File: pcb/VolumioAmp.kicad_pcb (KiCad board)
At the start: 2 copper layers, 136 x 71.2 mm, 81 parts, among them IC1 PCM2706, IC2 WM8804GEDS_V, J3 24v Input, Q1 DMP3013SFV-7, U1 74LVC1G07SE-7, U2 TPD4EUSB30, U3 TPD4EUSB30, U4 MagJack-A70-112-331N126, U5 FSUSB42MUX, U6 24AA02-OT, U7 AP64501SP-13, U8 LT1761-3.3, U9 MA12040PXUMA1

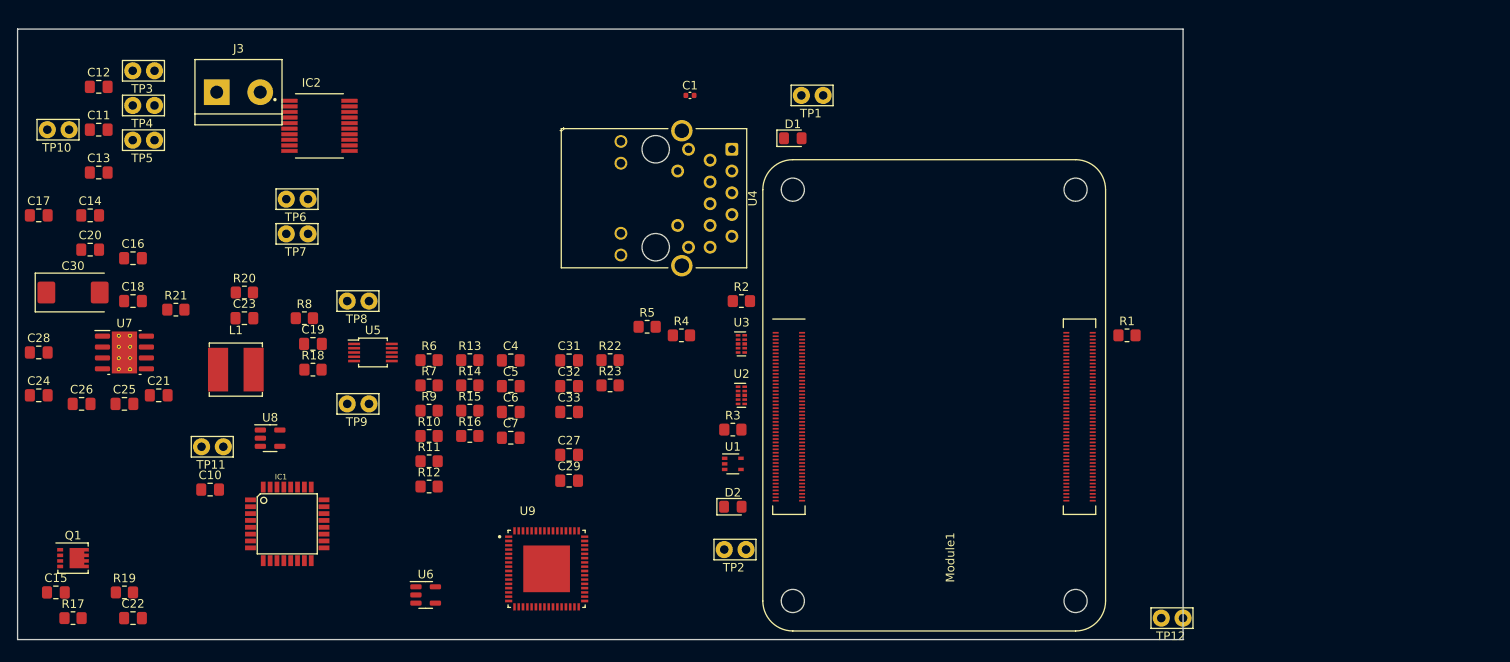
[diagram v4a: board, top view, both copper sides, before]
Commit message: - amp connected
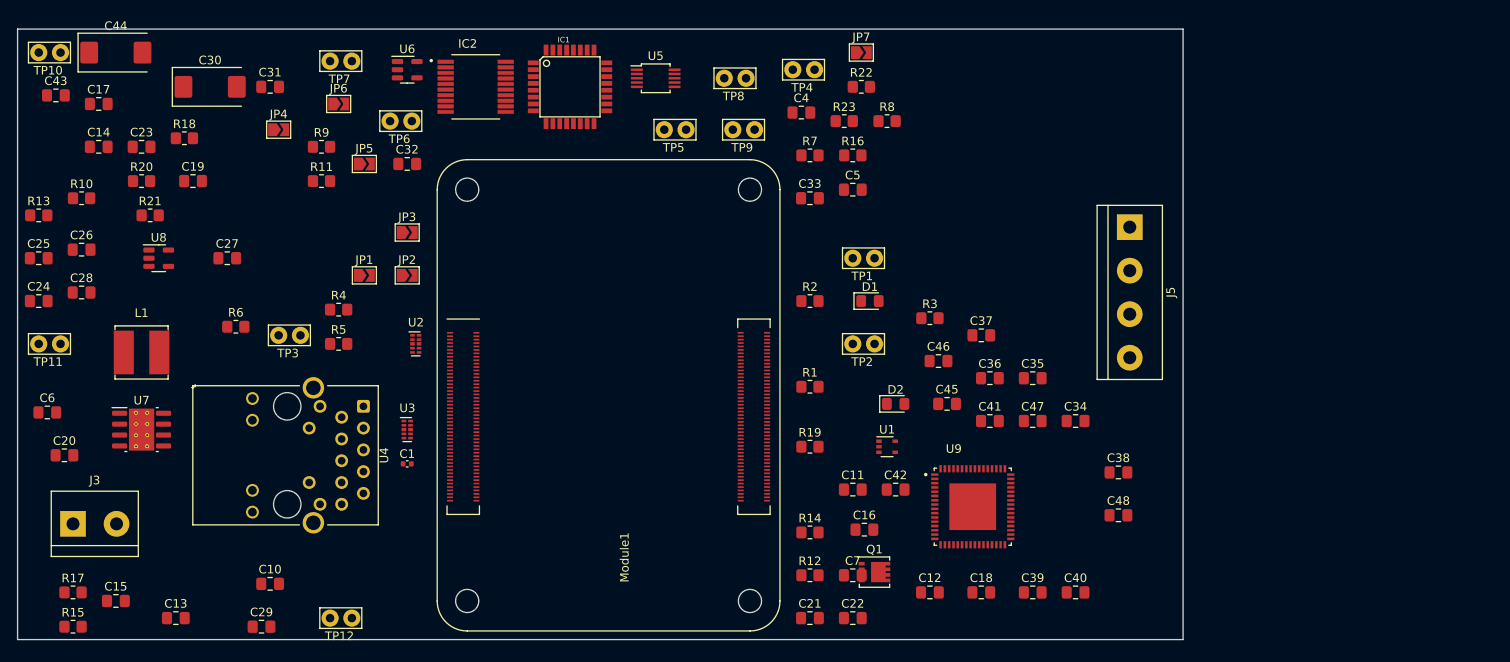
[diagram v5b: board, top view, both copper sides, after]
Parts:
- added C34: 1u, Capacitor_SMD:C_0805_2012Metric_Pad1.18x1.45mm_HandSolder, F.Cu at (157.0, 70.0)
- added C35: 1u, Capacitor_SMD:C_0805_2012Metric_Pad1.18x1.45mm_HandSolder, F.Cu at (152.0, 65.0)
- added C36: 1u, Capacitor_SMD:C_0805_2012Metric_Pad1.18x1.45mm_HandSolder, F.Cu at (147.0, 65.0)
- added C37: 100n, Capacitor_SMD:C_0805_2012Metric_Pad1.18x1.45mm_HandSolder, F.Cu at (146.0, 60.0)
- added C38: 1u, Capacitor_SMD:C_0805_2012Metric_Pad1.18x1.45mm_HandSolder, F.Cu at (162.0, 76.0)
- added C39: 1u, Capacitor_SMD:C_0805_2012Metric_Pad1.18x1.45mm_HandSolder, F.Cu at (152.0, 90.0)
- added C40: 1u, Capacitor_SMD:C_0805_2012Metric_Pad1.18x1.45mm_HandSolder, F.Cu at (157.0, 90.0)
- added C41: 1u, Capacitor_SMD:C_0805_2012Metric_Pad1.18x1.45mm_HandSolder, F.Cu at (147.0, 70.0)
- added C42: 1u, Capacitor_SMD:C_0805_2012Metric_Pad1.18x1.45mm_HandSolder, F.Cu at (136.0, 78.0)
- added C43: 1u, Capacitor_SMD:C_0805_2012Metric_Pad1.18x1.45mm_HandSolder, F.Cu at (38.0, 32.0)
- added C44: 470u, Capacitor_Tantalum_SMD:CP_EIA-7343-31_Kemet-D, F.Cu at (45.0, 27.0)
- added C45: 10u, Capacitor_SMD:C_0805_2012Metric_Pad1.18x1.45mm_HandSolder, F.Cu at (142.0, 68.0)
- added C46: 10u, Capacitor_SMD:C_0805_2012Metric_Pad1.18x1.45mm_HandSolder, F.Cu at (141.0, 63.0)
- added C47: 10u, Capacitor_SMD:C_0805_2012Metric_Pad1.18x1.45mm_HandSolder, F.Cu at (152.0, 70.0)
- added C48: 10u, Capacitor_SMD:C_0805_2012Metric_Pad1.18x1.45mm_HandSolder, F.Cu at (162.0, 81.0)
- added J5: Screw_Terminal_01x04, TerminalBlock:TerminalBlock_bornier-4_P5.08mm, F.Cu at (163.3, 47.4)
- added JP1: LRCK, Jumper:SolderJumper-2_P1.3mm_Open_TrianglePad1.0x1.5mm, F.Cu at (74.0, 53.0)
- added JP2: D, Jumper:SolderJumper-2_P1.3mm_Open_TrianglePad1.0x1.5mm, F.Cu at (79.0, 53.0)
- added JP3: BCK, Jumper:SolderJumper-2_P1.3mm_Open_TrianglePad1.0x1.5mm, F.Cu at (79.0, 48.0)
- added JP4: LRCK, Jumper:SolderJumper-2_P1.3mm_Open_TrianglePad1.0x1.5mm, F.Cu at (64.0, 36.0)
- added JP5: BCK, Jumper:SolderJumper-2_P1.3mm_Open_TrianglePad1.0x1.5mm, F.Cu at (74.0, 40.0)
- added JP6: MCK, Jumper:SolderJumper-2_P1.3mm_Open_TrianglePad1.0x1.5mm, F.Cu at (71.0, 33.0)
- added JP7: D, Jumper:SolderJumper-2_P1.3mm_Open_TrianglePad1.0x1.5mm, F.Cu at (132.0, 27.0)
- moved C12 113.5 mm to (140.0, 90.0)
- moved C18 104.7 mm to (146.0, 90.0)
- moved C11 97.5 mm to (131.0, 78.0)
- moved TP12 97.0 mm to (70.0, 93.0)
- moved Q1 93.5 mm to (133.5, 87.6)
- moved C16 91.0 mm to (132.4, 82.7)
- moved C22 84.0 mm to (131.0, 93.0)
- moved R19 81.8 mm to (126.0, 73.0)
- moved C21 80.3 mm to (126.0, 93.0)
- moved TP4 77.1 mm to (124.0, 29.0)
- moved R8 71.8 mm to (135.0, 35.0)
- moved TP5 62.0 mm to (109.0, 36.0)
- moved U6 61.3 mm to (79.0, 29.0)
- moved IC1 60.7 mm to (98.0, 31.0)
- moved R16 55.4 mm to (131.0, 39.0)
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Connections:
- net /CM4_Ethernet/GPIO27 renamed /Amplifier/AmpControl.~{CLIP}
- Module1 pad 44: /CM4_Ethernet/GPIO10 -> /Amplifier/AmpControl.~{MUTE}
- Module1 pad 46: /CM4_Ethernet/GPIO22 -> /Amplifier/AmpControl.~{ENABLE}
- Module1 pad 50: /CM4_Ethernet/GPIO17 -> /Amplifier/AmpControl.~{ERROR}
- U9 pad 1: Net-(U9-PVSS-Pad1) -> GND
- U9 pad 12: unconnected-(U9-CF0BN-Pad12) -> Net-(U9-CF0BN)
- U9 pad 13: Net-(U9-PVSS-Pad1) -> GND
- U9 pad 14: Net-(U9-PVSS-Pad1) -> GND
- U9 pad 15: unconnected-(U9-~{CLIP}-Pad15) -> /Amplifier/AmpControl.~{ENABLE}
- U9 pad 16: unconnected-(U9-~{ERROR}-Pad16) -> /Amplifier/AmpControl.~{ERROR}
- U9 pad 17: unconnected-(U9-AVDD-Pad17) -> GND
- U9 pad 18: unconnected-(U9-CMSE-Pad18) -> Net-(U9-CMSE)
- U9 pad 19: Net-(U9-AVSS-Pad19) -> GND
- U9 pad 2: Net-(U9-PVSS-Pad1) -> GND
- U9 pad 20: unconnected-(U9-CREF-Pad20) -> Net-(U9-CREF)
- U9 pad 21: unconnected-(U9-SCK-Pad21) -> /Amplifier/I2S.BCK
- U9 pad 22: unconnected-(U9-WS-Pad22) -> /Amplifier/I2S.LRCK
- U9 pad 23: unconnected-(U9-SD0-Pad23) -> /Amplifier/I2S.D
- U9 pad 25: Net-(U9-AVSS-Pad19) -> GND
- U9 pad 26: Net-(U9-DVSS-Pad26) -> GND
- U9 pad 27: unconnected-(U9-SCL-Pad27) -> /Amplifier/SCL
- U9 pad 28: unconnected-(U9-AD0-Pad28) -> GND
- U9 pad 29: unconnected-(U9-AD1-Pad29) -> GND
- U9 pad 3: unconnected-(U9-CF0AN-Pad3) -> Net-(U9-CF0AN)
- U9 pad 30: unconnected-(U9-SDA-Pad30) -> /Amplifier/SDA
- U9 pad 31: unconnected-(U9-CLKM/S-Pad31) -> GND
- U9 pad 32: unconnected-(U9-CLK-Pad32) -> /Amplifier/I2S.MCK
- U9 pad 33: unconnected-(U9-~{ENABLE}-Pad33) -> /Amplifier/AmpControl.~{ENABLE}
- U9 pad 34: unconnected-(U9-~{MUTE}-Pad34) -> /Amplifier/AmpControl.~{MUTE}
- U9 pad 35: Net-(U9-PVSS-Pad1) -> GND
- U9 pad 36: Net-(U9-PVSS-Pad1) -> GND
- U9 pad 37: unconnected-(U9-CF1BN-Pad37) -> Net-(U9-CF1BN)
- U9 pad 40: unconnected-(U9-CF1BP-Pad40) -> Net-(U9-CF1BP)
- U9 pad 41: Net-(U9-PVDD-Pad41) -> /Power/+12v
- U9 pad 42: Net-(U9-PVDD-Pad41) -> /Power/+12v
- U9 pad 43: unconnected-(U9-CF1AP-Pad43) -> Net-(U9-CF1AP)
- U9 pad 46: unconnected-(U9-CF1AN-Pad46) -> Net-(U9-CF1AN)
- U9 pad 47: Net-(U9-PVSS-Pad1) -> GND
- U9 pad 48: Net-(U9-PVSS-Pad1) -> GND
- U9 pad 50: unconnected-(U9-MSEL1-Pad50) -> GND
- U9 pad 51: unconnected-(U9-MSEL0-Pad51) -> /Amplifier/+5v
- U9 pad 52: unconnected-(U9-CGD1N-Pad52) -> Net-(U9-CGD1N)
- U9 pad 53: unconnected-(U9-CGD1P-Pad53) -> Net-(U9-CGD1P)
- U9 pad 54: unconnected-(U9-VGDC-Pad54) -> Net-(U9-VGDC)
- U9 pad 55: unconnected-(U9-DVDD-Pad55) -> /Amplifier/+5v
- U9 pad 56: unconnected-(U9-CDC-Pad56) -> Net-(U9-CDC)
- U9 pad 57: unconnected-(U9-CFDCP-Pad57) -> Net-(U9-CFDCP)
- U9 pad 58: unconnected-(U9-CFDCN-Pad58) -> Net-(U9-CFDCN)
- U9 pad 59: Net-(U9-DVSS-Pad26) -> GND
- U9 pad 6: unconnected-(U9-CF0AP-Pad6) -> Net-(U9-CF0AP)
- U9 pad 60: unconnected-(U9-CGD0P-Pad60) -> Net-(U9-CGD0P)
- U9 pad 61: unconnected-(U9-CGD0N-Pad61) -> Net-(U9-CGD0N)
- U9 pad 62: unconnected-(U9-CFGDP-Pad62) -> Net-(U9-CFGDP)
- U9 pad 63: unconnected-(U9-CFGDN-Pad63) -> Net-(U9-CFGDN)
- U9 pad 65: unconnected-(U9-EXP-Pad65) -> GND
- U9 pad 7: Net-(U9-PVDD-Pad41) -> /Power/+12v
- U9 pad 8: Net-(U9-PVDD-Pad41) -> /Power/+12v
- U9 pad 9: unconnected-(U9-CF0BP-Pad9) -> Net-(U9-CF0BP)

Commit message: - cleanup ERC errors
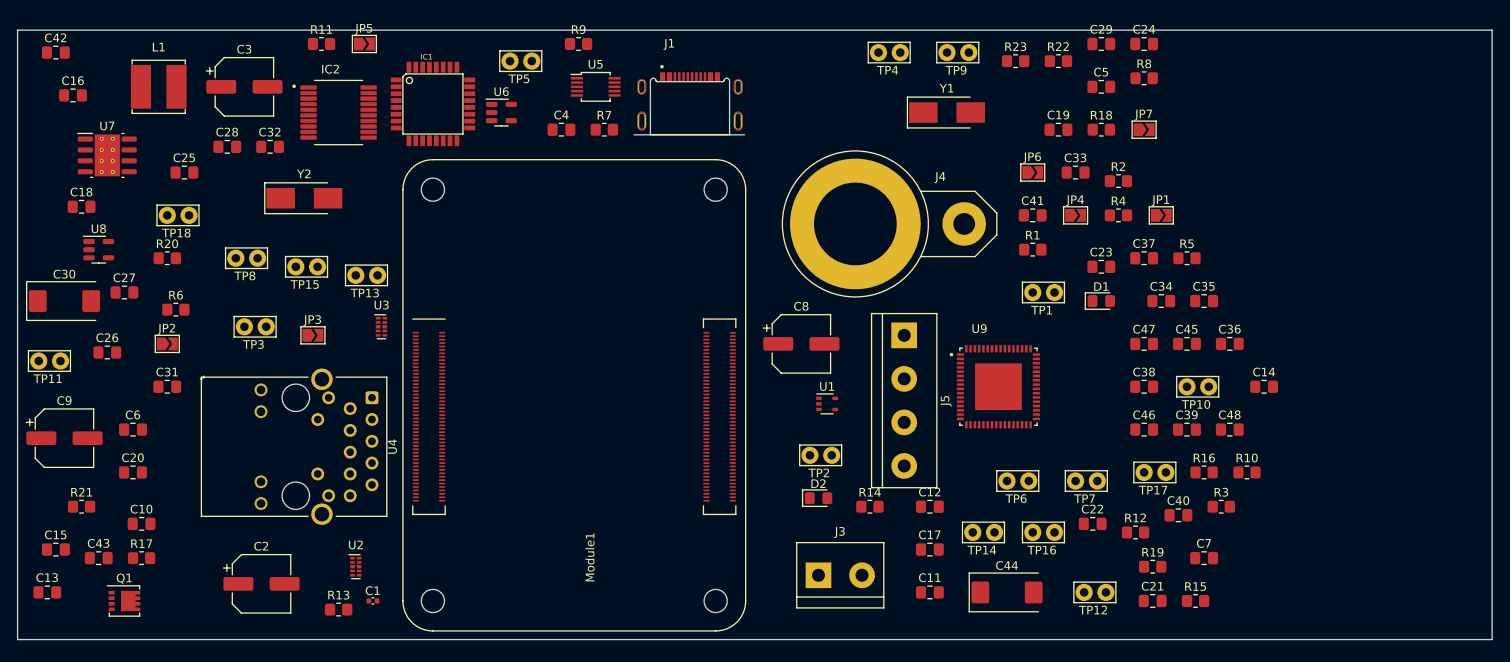
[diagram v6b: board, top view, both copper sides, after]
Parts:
- added C2: 1u, Capacitor_SMD:CP_Elec_6.3x7.7, F.Cu at (62.0, 89.0)
- added C3: 10u, Capacitor_SMD:CP_Elec_6.3x7.7, F.Cu at (60.0, 31.0)
- added C8: 100u, Capacitor_SMD:CP_Elec_6.3x7.7, F.Cu at (125.0, 61.0)
- added C9: 100u, Capacitor_SMD:CP_Elec_6.3x7.7, F.Cu at (39.0, 72.0)
- added J1: USB4500-03-0-A_REVA, Footprints:GCT_USB4500-03-0-A_REVA, F.Cu at (112.0, 35.0)
- added J4: Conn_Coaxial, Connector_Coaxial:BNC_PanelMountable_Vertical, F.Cu at (144.0, 47.0)
- added TP13: D, TestPoint:TestPoint_Bridge_Pitch2.54mm_Drill1.0mm, F.Cu at (73.0, 53.0)
- added TP14: LRCK, TestPoint:TestPoint_Bridge_Pitch2.54mm_Drill1.0mm, F.Cu at (145.0, 83.0)
- added TP15: BCK, TestPoint:TestPoint_Bridge_Pitch2.54mm_Drill1.0mm, F.Cu at (66.0, 52.0)
- added TP16: MCK, TestPoint:TestPoint_Bridge_Pitch2.54mm_Drill1.0mm, F.Cu at (152.0, 83.0)
- added TP17: D, TestPoint:TestPoint_Bridge_Pitch2.54mm_Drill1.0mm, F.Cu at (165.0, 76.0)
- added TP18: D, TestPoint:TestPoint_Bridge_Pitch2.54mm_Drill1.0mm, F.Cu at (51.0, 46.0)
- added Y1: 12Mhz, Crystal:Crystal_SMD_Abracon_ABM3-2Pin_5.0x3.2mm_HandSoldering, F.Cu at (142.0, 34.0)
- added Y2: 12Mhz, Crystal:Crystal_SMD_Abracon_ABM3-2Pin_5.0x3.2mm_HandSoldering, F.Cu at (67.0, 44.0)
- IC1: footprint Libraries:TQFP32-08 -> Footprints:TQFP32-08
- Module1: footprint CM4IO:Raspberry-Pi-4-Compute-Module -> Footprints:Raspberry-Pi-4-Compute-Module
- U4: footprint CM4IO:TRJG0926HENL -> Footprints:TRJG0926HENL
- moved R10 139.7 mm to (177.0, 76.0)
- moved TP10 139.6 mm to (170.0, 66.0)
- moved C14 138.9 mm to (179.0, 66.0)
- moved C24 132.4 mm to (165.0, 26.0)
- moved R15 131.0 mm to (171.0, 91.0)
- moved C44 121.6 mm to (149.0, 90.0)
- moved C29 119.3 mm to (160.0, 26.0)
- moved C18 114.2 mm to (41.0, 45.0)
- moved C23 112.9 mm to (160.0, 52.0)
- moved C42 110.5 mm to (38.0, 27.0)
- moved C17 110.1 mm to (140.0, 85.0)
- moved R18 107.0 mm to (160.0, 36.0)
- moved C16 105.3 mm to (40.0, 32.0)
- moved C19 101.2 mm to (155.0, 36.0)
- moved TP7 99.8 mm to (157.0, 77.0)
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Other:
- board size 136 x 71.2 mm -> 172.1 x 71.1 mm

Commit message: - pcb saved
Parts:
- moved C14 140.4 mm to (41.0, 40.0)
- moved TP10 132.7 mm to (39.0, 45.0)
- moved C24 119.5 mm to (56.0, 75.0)
- moved C29 117.6 mm to (46.0, 55.0)
- moved C2 117.5 mm to (163.0, 29.0)
- moved C16 116.3 mm to (139.0, 93.0)
- moved C11 115.7 mm to (43.0, 27.0)
- moved C21 113.9 mm to (59.0, 52.0)
- moved C23 110.8 mm to (51.0, 72.0)
- moved R19 110.2 mm to (60.0, 57.0)
- moved C45 110.0 mm to (39.0, 89.0)
- moved C17 105.0 mm to (41.0, 50.0)
- moved C12 101.0 mm to (54.0, 27.0)
- moved TP7 100.3 mm to (70.0, 27.0)
- moved TP5 98.5 mm to (186.0, 54.0)
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- renumbered C34 to C31, C35 to C32, C36 to C33, C37 to C34, C38 to C35, C39 to C36, C45 to C37, C46 to C38, C47 to C39, C48 to C40, C40 to C42, C42 to C43, C43 to C44, C44 to C45, C31 to C46, C32 to C47, C33 to C48, J5 to J4, J4 to J5
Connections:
- net /Amplifier/AmpControl.~{ERROR} renamed /Amplifier/AC.~{ERROR}
- net /Amplifier/AmpControl.~{MUTE} renamed /Amplifier/AC.~{MUTE}
- net /Power/+12v renamed /Amplifier/+24v
- net /USB_Sound/USB_N renamed /CM4_HighSpeed/USB2_N
- net /USB_Sound/USB_P renamed /CM4_HighSpeed/USB2_P
- C35 pad 2: /Amplifier/+5v -> /CM4_Ethernet/+5v
- JP1 pad 1: unconnected-(JP1-A-Pad1) -> /Amplifier/I2S.LRCK
- JP7 pad 2: unconnected-(JP7-B-Pad2) -> /Amplifier/I2S.D
- Module1 pad 46: /Amplifier/AmpControl.~{ENABLE} -> /Amplifier/AC.~{ENABLE}
- Module1 pad 48: /Amplifier/AmpControl.~{CLIP} -> /Amplifier/AC.~{CLIP}
- TP17 pad 1: /Amplifier/+5v -> /CM4_Ethernet/+5v
- U9 pad 15: /Amplifier/AmpControl.~{ENABLE} -> /Amplifier/AC.~{CLIP}
- U9 pad 24: unconnected-(U9-SD1-Pad24) -> GND
- U9 pad 33: /Amplifier/AmpControl.~{ENABLE} -> /Amplifier/AC.~{ENABLE}
- U9 pad 51: /Amplifier/+5v -> /CM4_Ethernet/+5v
- U9 pad 55: /Amplifier/+5v -> /CM4_Ethernet/+5v

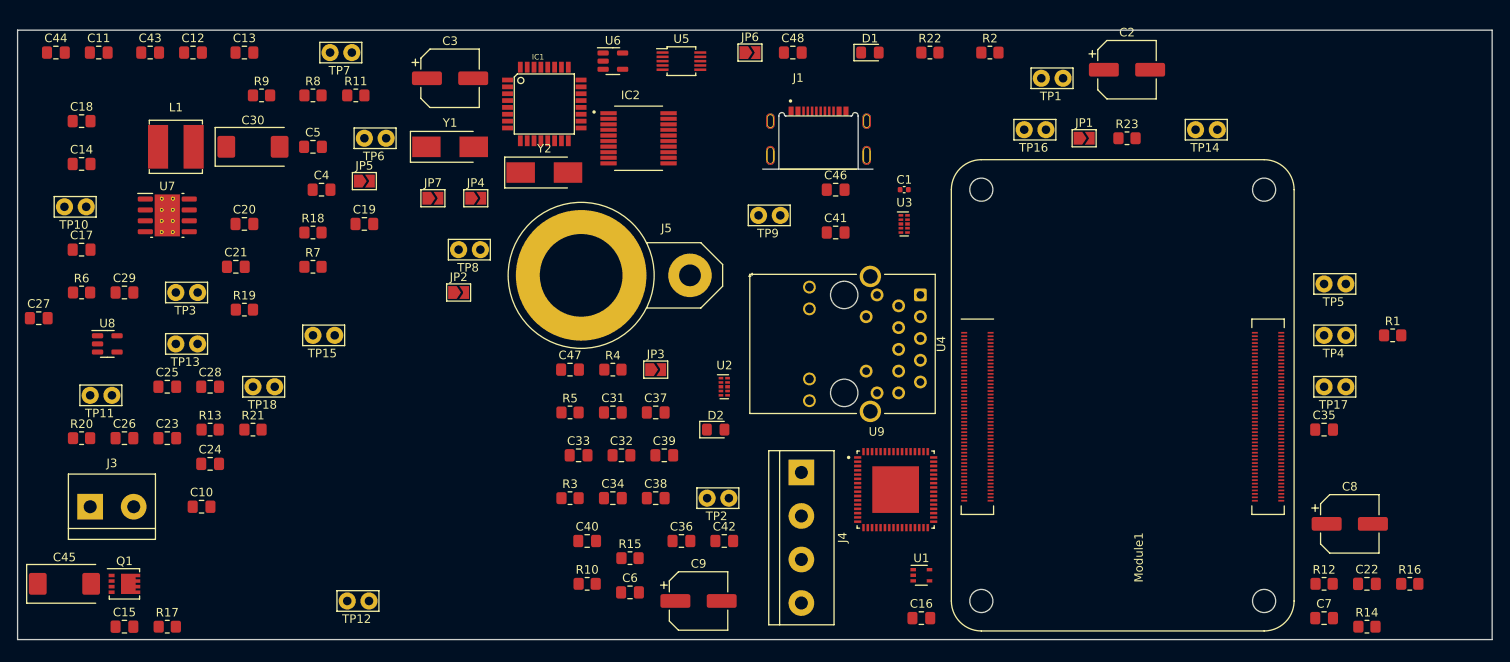
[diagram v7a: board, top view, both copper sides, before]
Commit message: - work in progress, changed rj45 connector
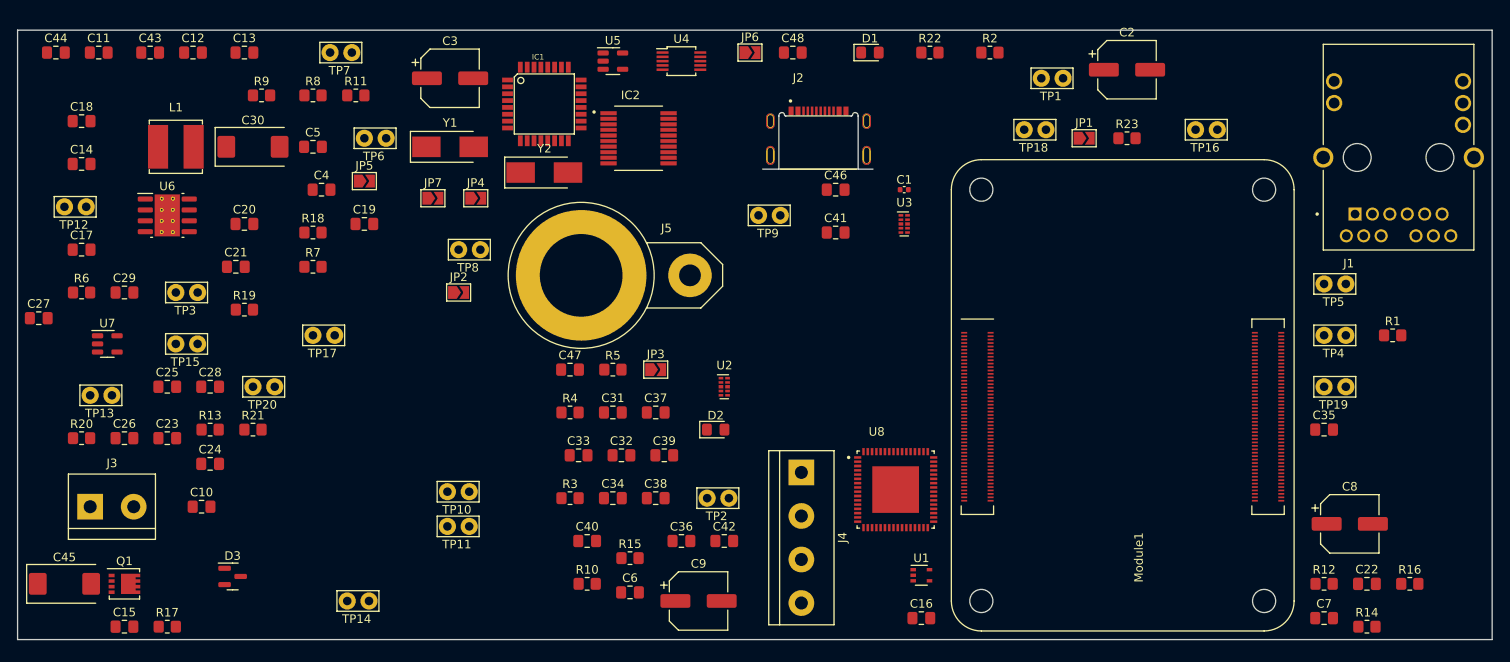
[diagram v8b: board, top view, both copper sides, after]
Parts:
- removed the U4 at (130.0, 61.0)
- added D3: MMBZ5242BLT3G, Package_TO_SOT_SMD:SOT-23, F.Cu at (58.6, 88.1)
- added J1: L829-1J1T-43, Footprints:BEL_L829-1J1T-43, F.Cu at (194.7, 39.2)
- added TP10: Out R, TestPoint:TestPoint_Bridge_Pitch2.54mm_Drill1.0mm, F.Cu at (83.7, 78.2)
- added TP11: Out L, TestPoint:TestPoint_Bridge_Pitch2.54mm_Drill1.0mm, F.Cu at (83.7, 82.3)
- renumbered J1 to J2, R5 to R4, R4 to R5, TP10 to TP12, TP11 to TP13, TP12 to TP14, TP13 to TP15, TP14 to TP16, TP15 to TP17, TP16 to TP18, TP17 to TP19, TP18 to TP20, U5 to U4, U6 to U5, U7 to U6, U8 to U7, U9 to U8
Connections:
- Module1 pad 78: /CM4_Ethernet/+3.3v -> Net-(Module1A-GPIO_VREF(1.8v/3.3v_Input))
- Module1 pad 84: /CM4_Ethernet/+3.3v -> Net-(Module1A-GPIO_VREF(1.8v/3.3v_Input))
- Module1 pad 86: /CM4_Ethernet/+3.3v -> Net-(Module1A-GPIO_VREF(1.8v/3.3v_Input))
